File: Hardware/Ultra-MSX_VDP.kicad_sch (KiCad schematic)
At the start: 6 parts, among them J18 Amphenol_L77HDE15SD1CH4RHNVGA, J19 Console5_SCART, J3 Ultra-VDP-daughter

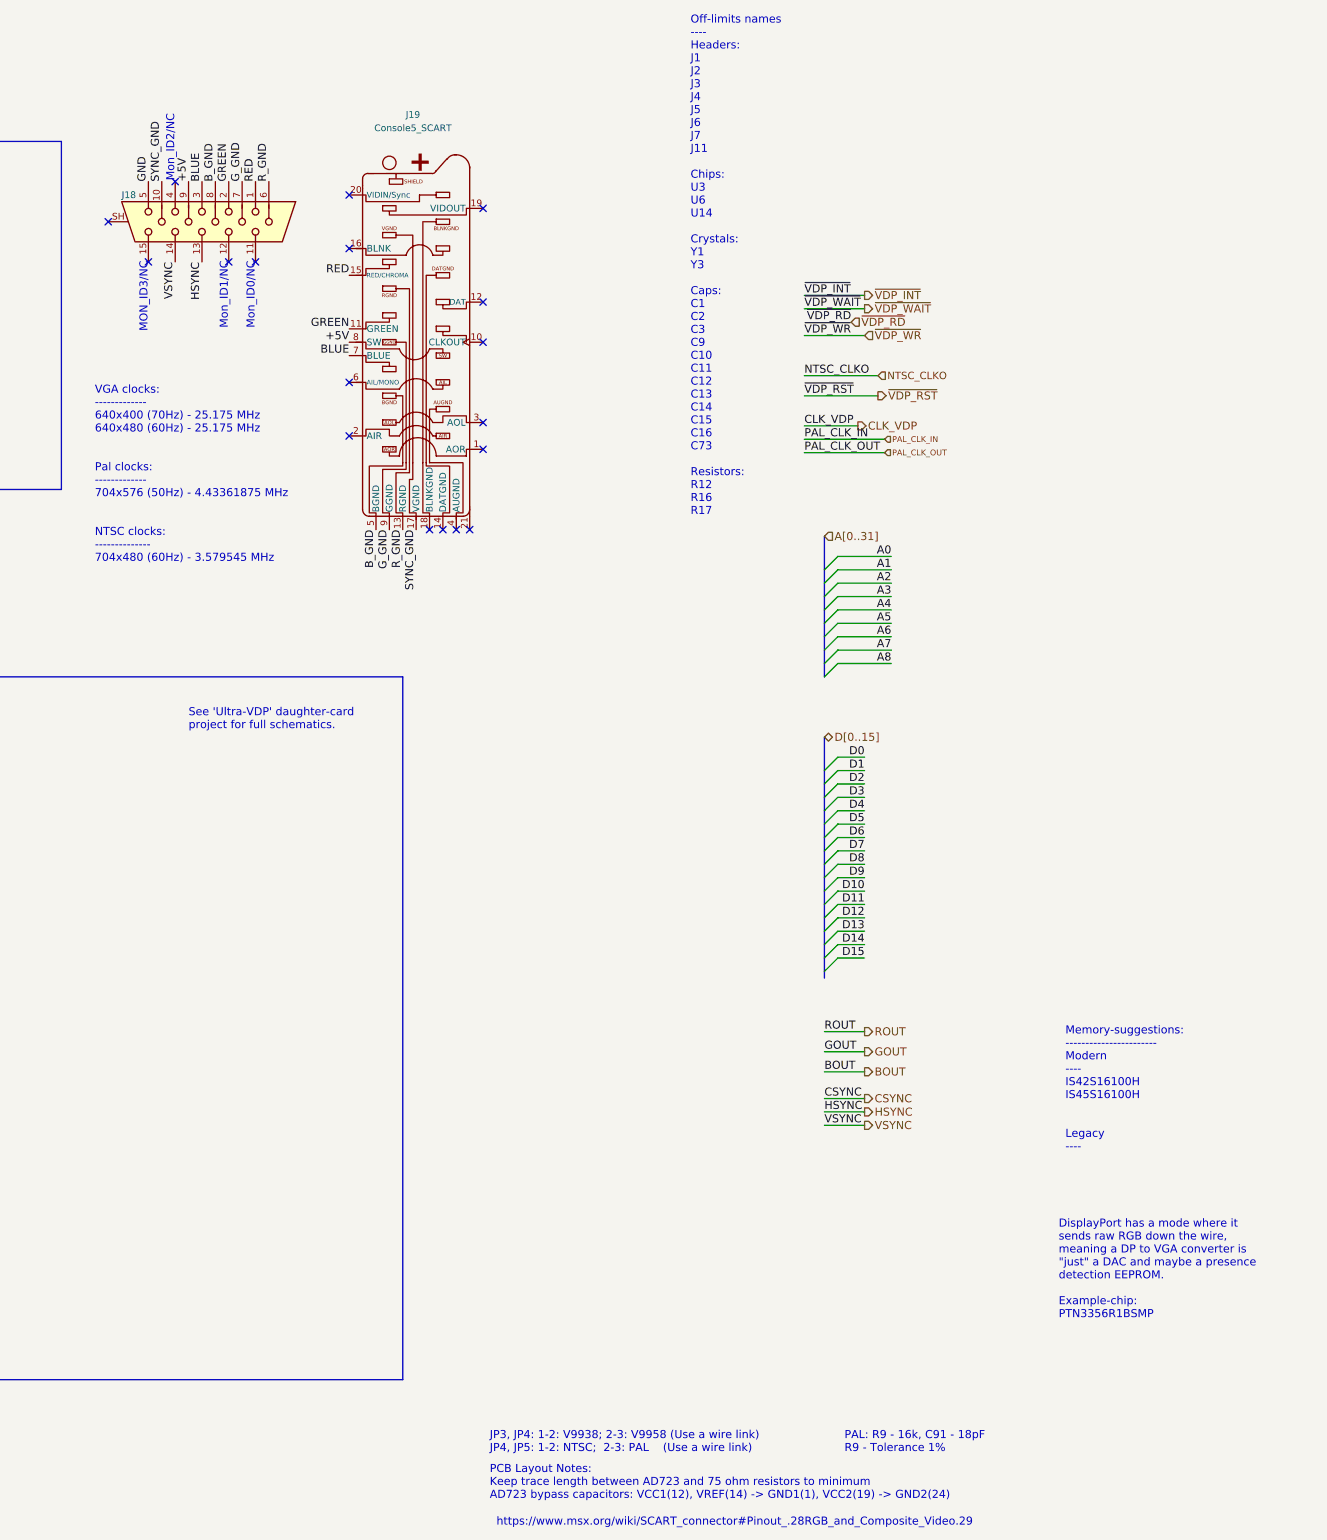
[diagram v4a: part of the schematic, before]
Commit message: Generated first PDF-files
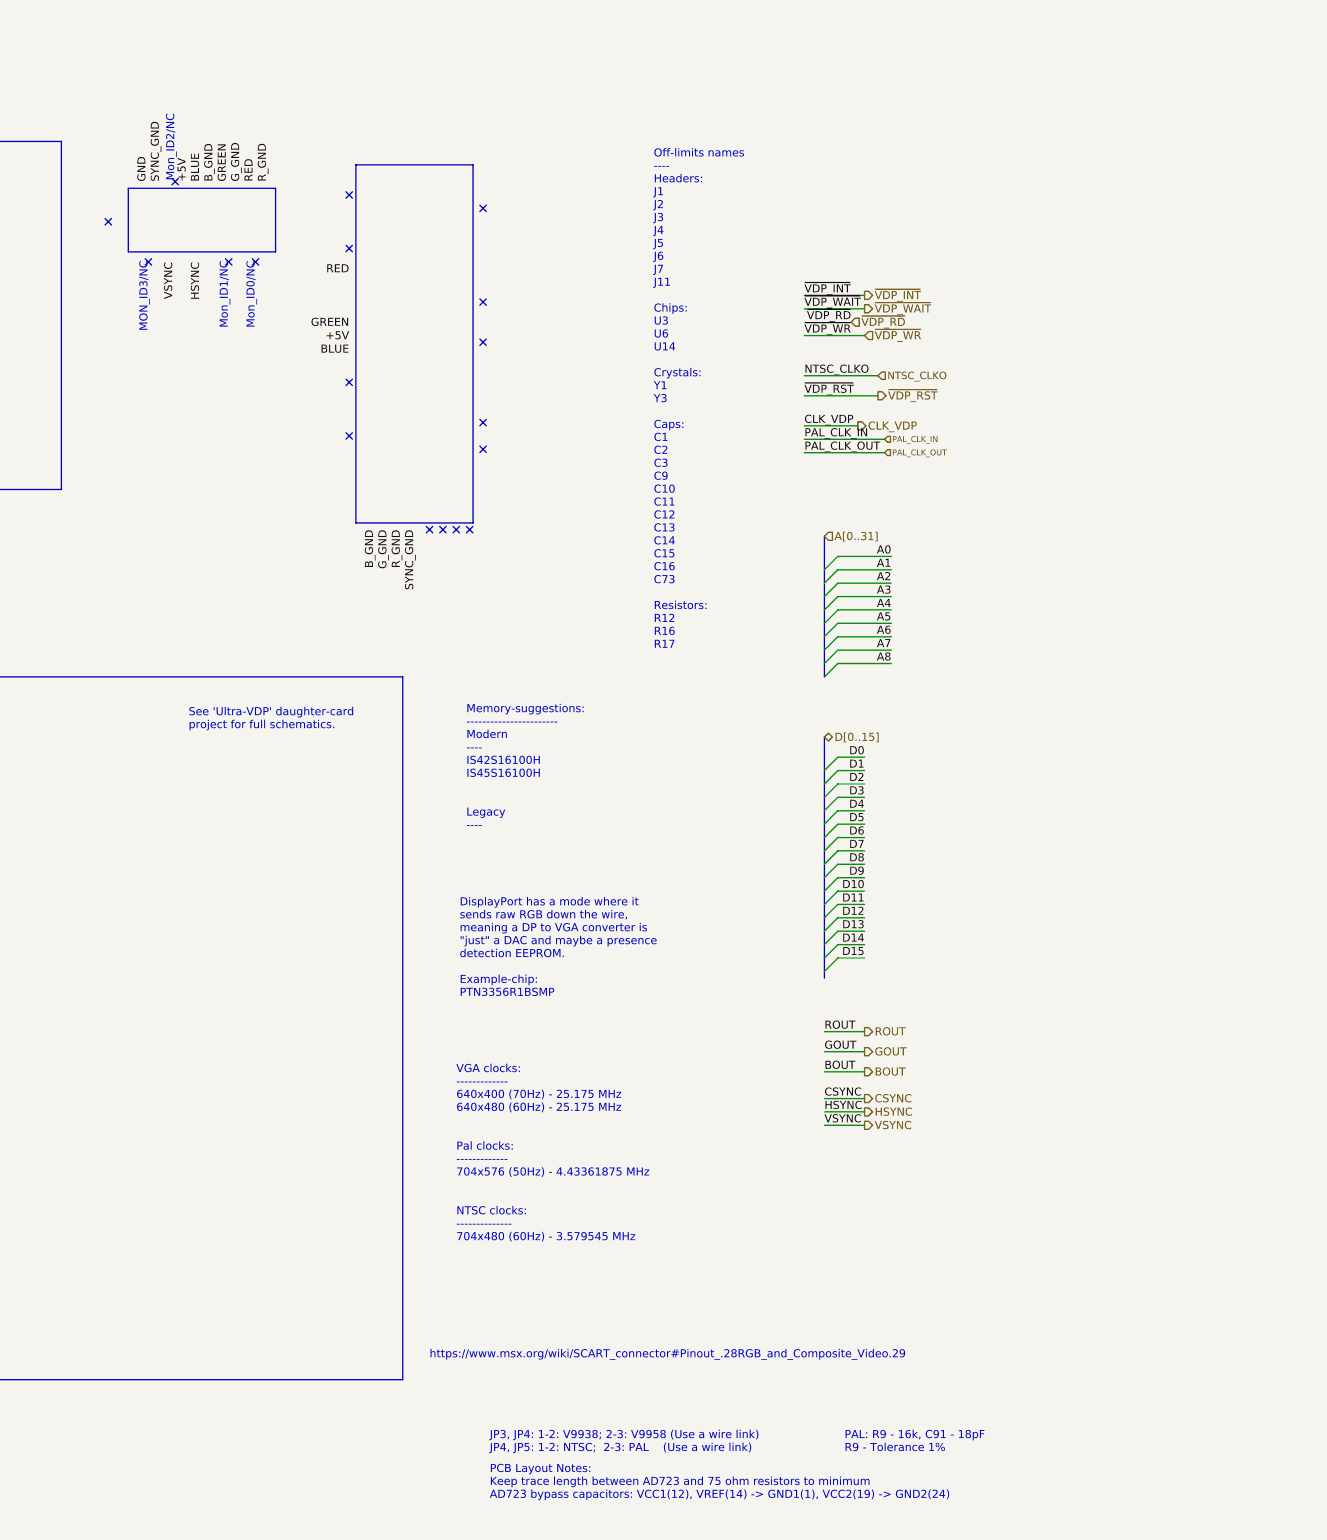
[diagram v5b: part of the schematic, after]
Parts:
- removed J18: Amphenol_L77HDE15SD1CH4RHNVGA, LRJ:DSUB-Amphenol_L77HDE15SD1CH4RHNVGA, symbol LRJ-parts:Amphenol_L77HDE15SD1CH4RHNVGA
- removed J19: Console5_SCART, LRJ:SCART-21_Female_Horizontal_P1.905x2.54mm_EdgePinOffset10.7mm, symbol LRJ-parts:Console5_SCART
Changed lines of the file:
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@@
     (stroke (width 0) (type default) (color 0 0 0 0))
   )
+  (polyline (pts (xy 250.19 29.21) (xy 250.19 41.275))
+    (stroke (width 0) (type default) (color 0 0 0 0))
+  )
   (wire (pts (xy 26.67 144.78) (xy 26.67 139.7))
     (stroke (width 0) (type default) (color 0 0 0 0))
@@
     (stroke (width 0) (type default) (color 0 0 0 0))
   )
+  (polyline (pts (xy 293.37 24.765) (xy 315.595 24.765))
+    (stroke (width 0) (type default) (color 0 0 0 0))
+  )
   (polyline (pts (xy 100.33 41.91) (xy 172.72 41.91))
     (stroke (width 0) (type default) (color 0 0 0 0))
@@
     (stroke (width 0) (type default) (color 0 0 0 0))
   )
+  (polyline (pts (xy 293.37 92.71) (xy 315.595 92.71))
+    (stroke (width 0) (type default) (color 0 0 0 0))
+  )
   (wire (pts (xy 388.62 74.295) (xy 378.46 74.295))
     (stroke (width 0) (type default) (color 0 0 0 0))
@@
     (stroke (width 0) (type default) (color 0 0 0 0))
   )
+  (polyline (pts (xy 315.595 92.71) (xy 315.595 24.765))
+    (stroke (width 0) (type default) (color 0 0 0 0))
+  )
   (wire (pts (xy 26.67 76.2) (xy 26.67 139.7))
     (stroke (width 0) (type default) (color 0 0 0 0))
@@
     (stroke (width 0.5) (type solid) (color 0 0 0 0))
   )
+  (polyline (pts (xy 293.37 24.765) (xy 293.37 92.71))
+    (stroke (width 0) (type default) (color 0 0 0 0))
+  )
   (wire (pts (xy 36.83 99.06) (xy 45.72 99.06))
     (stroke (width 0) (type default) (color 0 0 0 0))
@@
     (stroke (width 0) (type default) (color 0 0 0 0))
   )
+  (polyline (pts (xy 250.19 41.275) (xy 278.13 41.275))
+    (stroke (width 0) (type default) (color 0 0 0 0))
+  )
   (wire (pts (xy 26.67 76.2) (xy 26.67 71.12))
     (stroke (width 0) (type default) (color 0 0 0 0))
@@
     (stroke (width 0) (type default) (color 0 0 0 0))
   )
+  (polyline (pts (xy 278.13 41.275) (xy 278.13 29.21))
+    (stroke (width 0) (type default) (color 0 0 0 0))
+  )
   (wire (pts (xy 389.89 57.15) (xy 378.46 57.15))
     (stroke (width 0) (type default) (color 0 0 0 0))
@@
     (stroke (width 0) (type default) (color 0 0 0 0))
   )
+  (polyline (pts (xy 250.19 29.21) (xy 278.13 29.21))
+    (stroke (width 0) (type default) (color 0 0 0 0))
+  )
   (wire (pts (xy 384.81 170.18) (xy 389.89 170.18))
     (stroke (width 0) (type default) (color 0 0 0 0))
@@
   )
   (text "Memory-suggestions:\n-----------------------\nModern\n----\nIS42S16100H\nIS45S16100H\n\n\nLegacy\n----"
-    (at 427.99 212.09 0)
+    (at 314.325 151.13 0)
     (effects (font (size 1.524 1.524)) (justify left bottom))
   )
@@
   )
   (text "DisplayPort has a mode where it \nsends raw RGB down the wire, \nmeaning a DP to VGA converter is \n\"just\" a DAC and maybe a presence \ndetection EEPROM.\n\nExample-chip:\nPTN3356R1BSMP"
-    (at 426.72 243.84 0)
+    (at 313.055 182.88 0)
     (effects (font (size 1.524 1.524)) (justify left bottom))
   )
@@
   )
   (text "Off-limits names\n----\nHeaders:\nJ1\nJ2\nJ3\nJ4\nJ5\nJ6\nJ7\nJ11\n\nChips:\nU3\nU6\nU14\n\nCrystals:\nY1\nY3\n\nCaps:\nC1\nC2\nC3\nC9\nC10\nC11\nC12\nC13\nC14\nC15\nC16\nC73\n\nResistors:\nR12\nR16\nR17"
-    (at 356.87 91.44 0)
+    (at 349.885 116.84 0)
     (effects (font (size 1.524 1.524)) (justify left bottom))
   )
   (text "VGA clocks:\n-------------\n640x400 (70Hz) - 25.175 MHz\n640x480 (60Hz) - 25.175 MHz\n\n\nPal clocks:\n-------------\n704x576 (50Hz) - 4.43361875 MHz\n\n\nNTSC clocks:\n--------------\n704x480 (60Hz) - 3.579545 MHz"
-    (at 243.84 100.33 0)
+    (at 312.42 229.235 0)
     (effects (font (size 1.524 1.524)) (justify left bottom))
   )
@@
   )
   (text "https://www.msx.org/wiki/SCART_connector#Pinout_.28RGB_and_Composite_Video.29"
-    (at 320.04 283.21 0)
+    (at 307.34 251.46 0)
     (effects (font (size 1.524 1.524)) (justify left bottom))
   )
@@
     (effects (font (size 1.524 1.524)) (justify left))
   )
-  (symbol (lib_id "LRJ-parts:Amphenol_L77HDE15SD1CH4RHNVGA") (at 264.16 35.56 270) (unit 1)
-    (in_bom yes) (on_board yes)
-    (property "Reference" "J18" (id 0) (at 248.92 30.48 90)
-      (effects (font (size 1.27 1.27)) (justify left))
-    )
-    (property "Value" "Amphenol_L77HDE15SD1CH4RHNVGA" (id 1) (at 274.32 40.64 90)
-      (effects (font (size 1.27 1.27)) (justify left) hide)
-    )
-    (property "Footprint" "LRJ:DSUB-Amphenol_L77HDE15SD1CH4RHNVGA" (id 2) (at 259.08 78.74 0)
-      (effects (font (size 1.27 1.27)) hide)
-    )
-    (property "Datasheet" "https://www.mouser.se/datasheet/2/18/1/HD_high_density-1501066.pdf" (id 3) (at 250.19 92.71 0)
-      (effects (font (size 1.27 1.27)) hide)
-    )
-    (property "Mouser detail page" "https://www.mouser.se/ProductDetail/Amphenol-Commercial-Products/L77HDE15SD1CH4RHNVGA?qs=%2Fha2pyFaduiXRb9hzG6iBJ8i6gpx1OJm0bJEXIQ5bRyeuKuUIzRFk%2FAFOZs1tJ8cWJdHd0bs6Y8%3D" (id 4) (at 262.89 152.4 0)
-      (effects (font (size 1.27 1.27)) hide)
-    )
-    (property "Price" " 1,38 € " (id 5) (at 254 59.69 0)
-      (effects (font (size 1.27 1.27)) hide)
-    )
-    (pin "1")
-    (pin "10")
-    (pin "11")
-    (pin "12")
-    (pin "13")
-    (pin "14")
-    (pin "15")
-    (pin "2")
-    (pin "3")
-    (pin "4")
-    (pin "5")
-    (pin "6")
-    (pin "7")
-    (pin "8")
-    (pin "9")
-    (pin "SH")
-  )
   (symbol (lib_id "Device:C_Polarized") (at 124.46 31.75 90) (unit 1)
     (in_bom yes) (on_board yes)
@@
     (pin "1")
   )
-  (symbol (lib_id "LRJ-parts:Console5_SCART") (at 304.8 58.42 0) (unit 1)
-    (in_bom yes) (on_board yes) (fields_autoplaced)
-    (property "Reference" "J19" (id 0) (at 304.1967 15.24 0))
-    (property "Value" "Console5_SCART" (id 1) (at 304.1967 17.78 0))
-    (property "Footprint" "LRJ:SCART-21_Female_Horizontal_P1.905x2.54mm_EdgePinOffset10.7mm" (id 2) (at 364.49 59.69 0)
-      (effects (font (size 1.27 1.27)) hide)
-    )
-    (property "Datasheet" "https://console5.com/store/female-scart-jp21-through-hole-pcb-mount-21-pin-connector-right-angle.html#" (id 3) (at 303.53 52.07 0)
-      (effects (font (size 1.27 1.27)) hide)
-    )
-    (property "Manufacturer" "Console5" (id 4) (at 332.74 50.8 0)
-      (effects (font (size 1.524 1.524)) hide)
-    )
-    (property "MPN" "N/A" (id 5) (at 337.82 55.88 0)
-      (effects (font (size 1.524 1.524)) hide)
-    )
-    (pin "1")
-    (pin "10")
-    (pin "11")
-    (pin "12")
-    (pin "13")
-    (pin "14")
-    (pin "15")
-    (pin "16")
-    (pin "17")
-    (pin "18")
-    (pin "19")
-    (pin "2")
-    (pin "20")
-    (pin "21")
-    (pin "3")
-    (pin "4")
-    (pin "5")
-    (pin "6")
-    (pin "7")
-    (pin "8")
-    (pin "9")
-  )
   (symbol (lib_id "Device:C_Polarized") (at 124.46 36.83 90) (unit 1)
